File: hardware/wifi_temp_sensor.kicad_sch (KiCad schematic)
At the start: 12 parts, among them J1 USB_B_Mini, J2 ESP8266, J3 TempSensor, J4 Prog, J5 Display, SW1 BootMode, U2 AZ1117-3.3

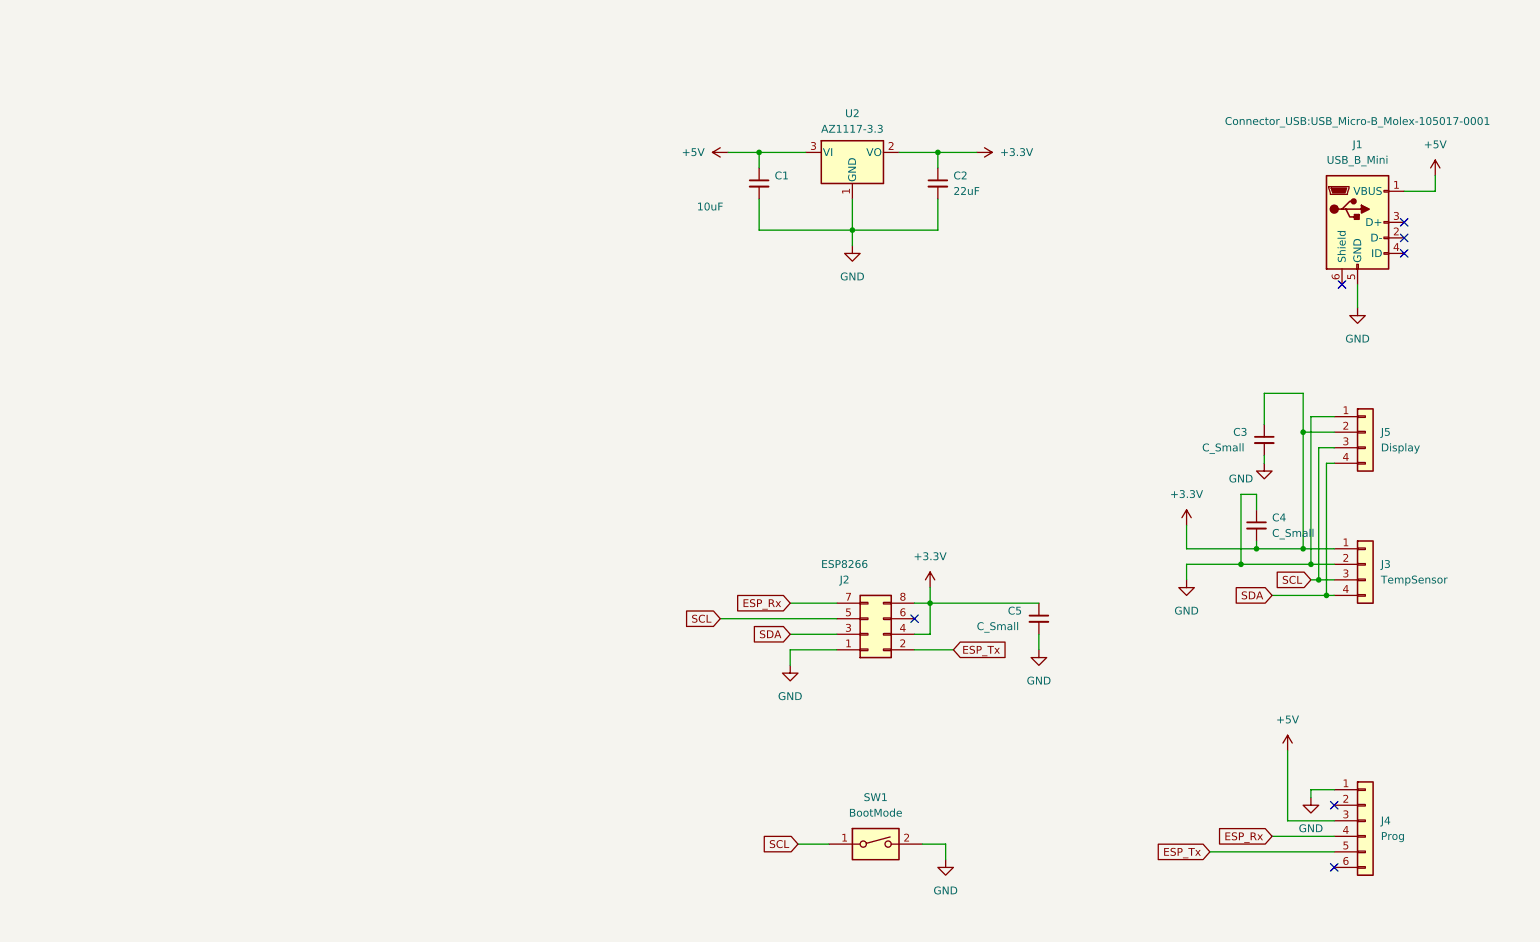
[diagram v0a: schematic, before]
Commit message: Added in USB C Port to replace USB micro
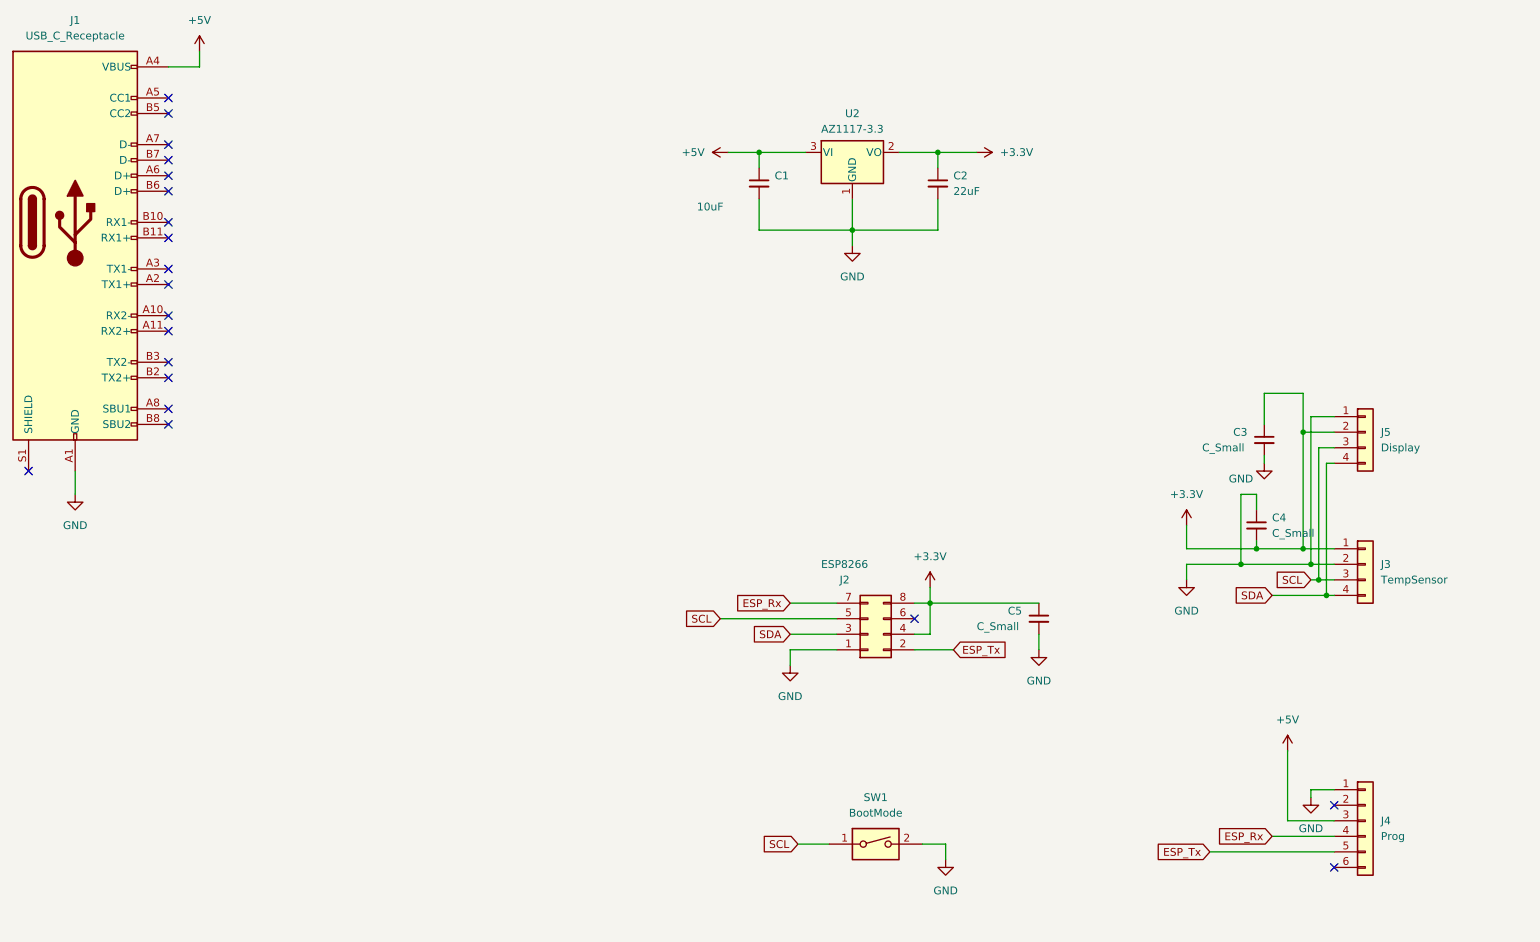
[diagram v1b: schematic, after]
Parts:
- removed J1: USB_B_Mini, Connector_USB:USB_Micro-B_Molex-105017-0001, symbol Connector:USB_B_Mini
- added J1: USB_C_Receptacle, Connector_USB:USB_C_Receptacle_GCT_USB4105-xx-A_16P_TopMnt_Horizontal, symbol Connector:USB_C_Receptacle
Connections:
- net +5V: now also J1.A4 (VBUS), J1.A9 (VBUS), J1.B4 (VBUS), J1.B9 (VBUS)
- net GND: now also J1.A1 (GND), J1.A12 (GND), J1.B1 (GND), J1.B12 (GND)
- no-connect marks 7 -> 20

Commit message: Don't really remember
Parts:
- added U1: CH340T, Package_SO:SSOP-20_5.3x7.2mm_P0.65mm, symbol Interface_USB:CH340T
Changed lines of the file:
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@@
+	)
+	(symbol
+		(lib_id "Interface_USB:CH340T")
+		(at 50.8 143.51 0)
+		(unit 1)
+		(exclude_from_sim no)
+		(in_bom yes)
+		(on_board yes)
+		(dnp no)
+		(fields_autoplaced yes)
+		(property "Reference" "U1"
+			(at 52.9941 163.83 0)
+			(effects
+				(font
+					(size 1.27 1.27)
+				)
+				(justify left)
+			)
+		)
+		(property "Value" "CH340T"
+			(at 52.9941 166.37 0)
+			(effects
+				(font
+					(size 1.27 1.27)
+				)
+				(justify left)
+			)
+		)
+		(property "Footprint" "Package_SO:SSOP-20_5.3x7.2mm_P0.65mm"
+			(at 73.66 163.83 0)
+			(effects
+				(font
+					(size 1.27 1.27)
+				)
+				(hide yes)
+			)
+		)
+		(property "Datasheet" "https://cdn.sparkfun.com/datasheets/Dev/Arduino/Other/CH340DS1.PDF"
+			(at 44.45 121.92 0)
+			(effects
+				(font
+					(size 1.27 1.27)
+				)
+				(hide yes)
+			)
+		)
+		(property "Description" "USB serial converter, UART, SSOP-20"
+			(at 50.8 143.51 0)
+			(effects
+				(font
+					(size 1.27 1.27)
+				)
+				(hide yes)
+			)
+		)
+		(pin "3"
+		)
+		(pin "13"
+		)
+		(pin "5"
+		)
+		(pin "18"
+		)
+		(pin "14"
+		)
+		(pin "17"
+		)
+		(pin "1"
+		)
+		(pin "12"
+		)
+		(pin "11"
+		)
+		(pin "10"
+		)
+		(pin "9"
+		)
+		(pin "8"
+		)
+		(pin "6"
+		)
+		(pin "4"
+		)
+		(pin "7"
+		)
+		(pin "2"
+		)
+		(pin "16"
+		)
+		(pin "19"
+		)
+		(pin "20"
+		)
+		(pin "15"
+		)
+		(instances
+			(project ""
+				(path "/f6c77997-b71a-421e-9dbe-7ca9e2d5ccfe"
+					(reference "U1")
+					(unit 1)
+				)
+			)
+		)
 	)
 	(symbol
